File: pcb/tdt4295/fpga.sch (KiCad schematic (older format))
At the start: 44 parts, among them J101 FPGA__debug, U101 S25FL127SABMFV101, U102 XC7A100T-FTG256-tdt4295

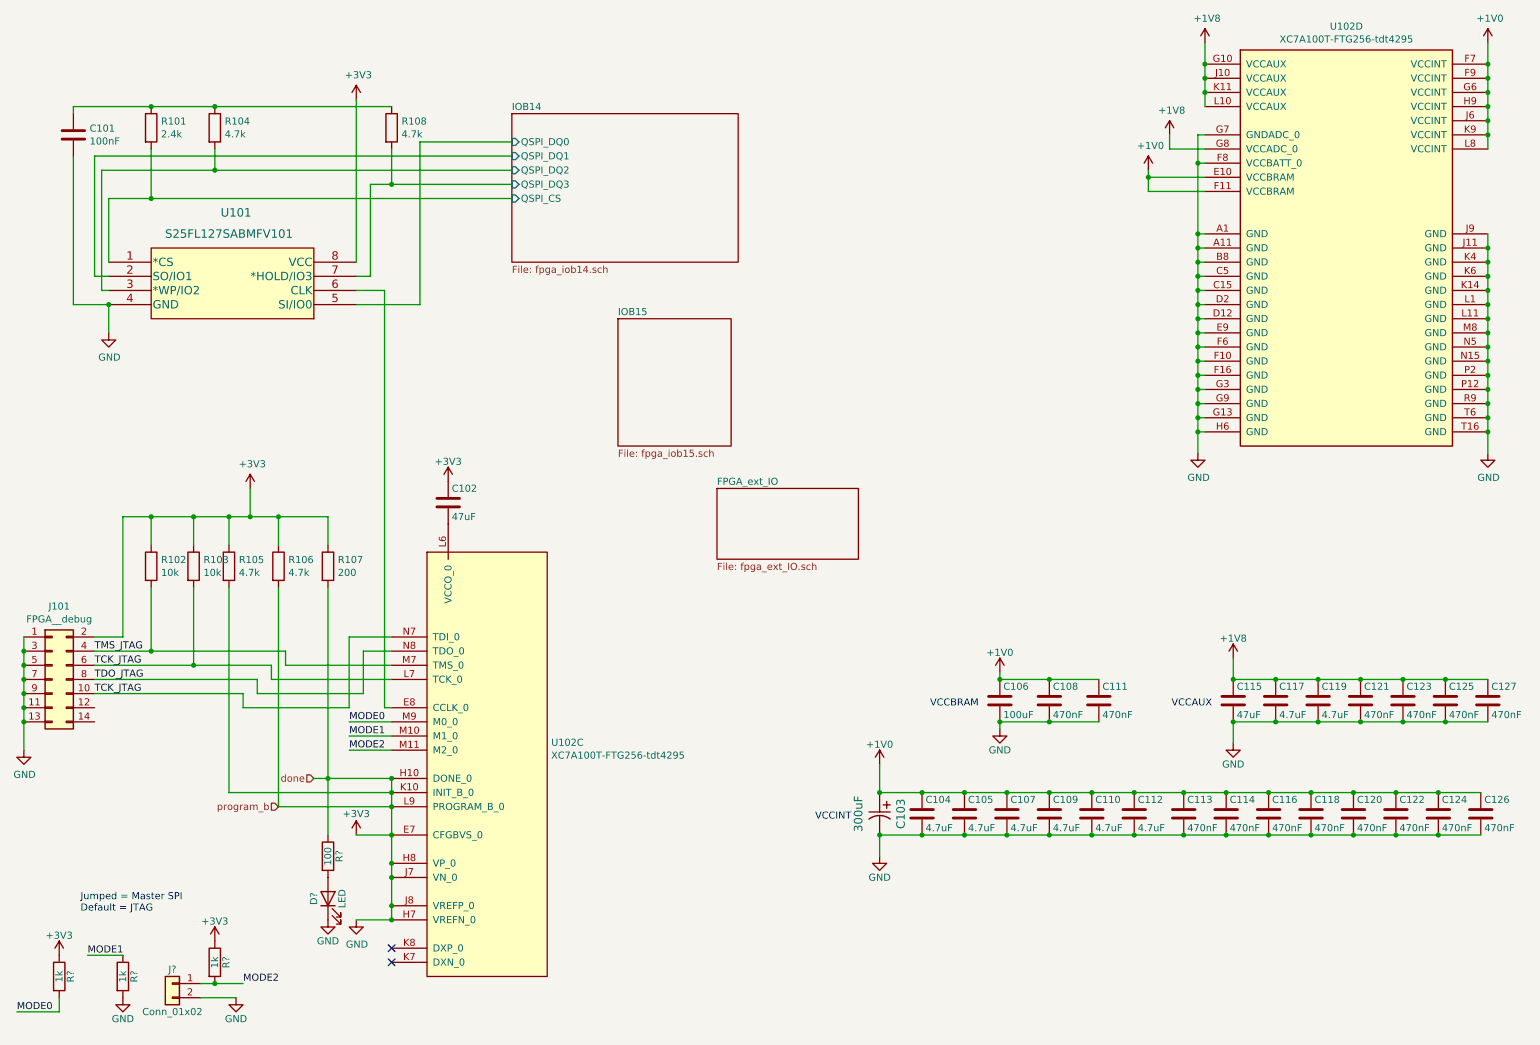
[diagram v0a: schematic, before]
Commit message: associate (most) symbols with footprints
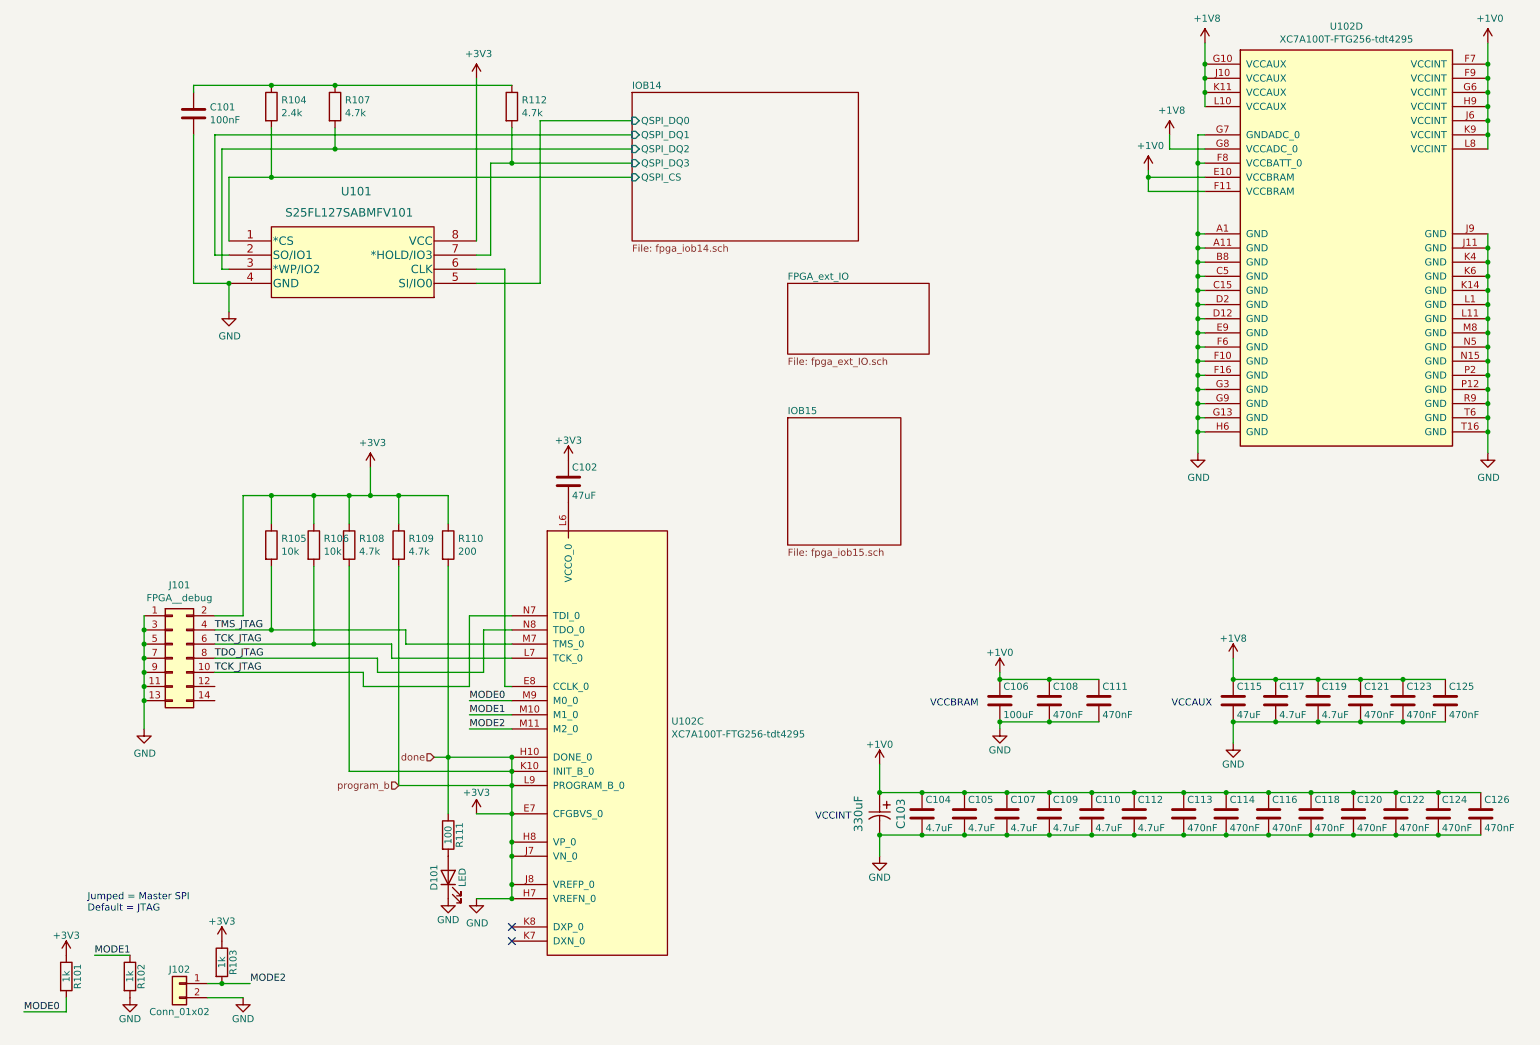
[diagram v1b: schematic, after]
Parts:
- removed C127: 470nF, symbol Device:C
- C102: footprint (none) -> Capacitor_SMD:C_1210_3225Metric_Pad1.33x2.70mm_HandSolder; Component name (none) -> GRM32ER71A476ME15L
- C103: value 300uF -> 330uF
- C108, C111, C113, C114, C116, C118, C120, C121, C122, C123, C124, C125, C126: footprint (none) -> Capacitor_SMD:C_0603_1608Metric_Pad1.08x0.95mm_HandSolder; Component name (none) -> GRM188R71C474KA88D
- D101: renamed from D?; footprint (none) -> Diode_SMD:D_0805_2012Metric_Pad1.15x1.40mm_HandSolder
- J102: renamed from J?; footprint (none) -> Connector_PinHeader_2.54mm:PinHeader_1x02_P2.54mm_Vertical
- R101, R102, R103: renamed from R?; footprint (none) -> Resistor_SMD:R_0402_1005Metric_Pad0.72x0.64mm_HandSolder; Component name (none) -> RR0510P-102-D
- R104: renamed from R101; footprint (none) -> Resistor_SMD:R_0805_2012Metric_Pad1.20x1.40mm_HandSolder; Component name (none) -> ERA-6AED242V
- R105: renamed from R102; footprint (none) -> Resistor_SMD:R_0805_2012Metric_Pad1.20x1.40mm_HandSolder; Component name (none) -> RR1220P-103-D
- R106: renamed from R103; footprint (none) -> Resistor_SMD:R_0805_2012Metric_Pad1.20x1.40mm_HandSolder; Component name (none) -> RR1220P-103-D
- R107: renamed from R104; footprint (none) -> Resistor_SMD:R_0603_1608Metric_Pad0.98x0.95mm_HandSolder; Component name (none) -> RG1608P-472-B-T5
- R108: renamed from R105; footprint (none) -> Resistor_SMD:R_0603_1608Metric_Pad0.98x0.95mm_HandSolder; Component name (none) -> RG1608P-472-B-T5
- R109: renamed from R106; footprint (none) -> Resistor_SMD:R_0603_1608Metric_Pad0.98x0.95mm_HandSolder; Component name (none) -> RG1608P-472-B-T5
- R110: renamed from R107; footprint (none) -> Resistor_SMD:R_0805_2012Metric_Pad1.20x1.40mm_HandSolder; Component name (none) -> RNCF0805TKY200R
- R111: renamed from R?; footprint (none) -> Resistor_SMD:R_0805_2012Metric_Pad1.20x1.40mm_HandSolder; Component name (none) -> TNPW0805100RBEEA
- R112: renamed from R108; footprint (none) -> Resistor_SMD:R_0603_1608Metric_Pad0.98x0.95mm_HandSolder; Component name (none) -> RG1608P-472-B-T5
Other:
- moved on the sheet: C101, C102, D101, J101, J102, R101, R102, R103, R104, R105, R106, R107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

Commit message: add final footprints, tweak VGA output
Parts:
- C101: footprint (none) -> Resistor_SMD:R_0402_1005Metric_Pad0.72x0.64mm_HandSolder; Component name (none) -> CL05B104KA5NNNC
- C103: footprint CAPMP7.6X4.3_1.9N_KEM -> T520V337M2R5ATE025-footprint:T520V337M2R5ATE025
- J101: footprint Connector_PinHeader_1.00mm:PinHeader_2x07_P1.00mm_Vertical -> Connector_PinHeader_2.54mm:PinHeader_1x02_P2.54mm_Vertical
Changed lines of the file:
@@
 F 0 "C103" H 6750 6250 60  0000 C CNN
 F 1 "330uF" H 6750 5950 60  0000 C CNN
-F 2 "CAPMP7.6X4.3_1.9N_KEM" H 6750 5740 60  0001 C CNN
+F 2 "T520V337M2R5ATE025-footprint:T520V337M2R5ATE025" H 6750 5740 60  0001 C CNN
 F 3 "" H 6600 6100 60  0000 C CNN
 F 4 "T520V337M2R5ATE025" H 6600 6100 50  0001 C CNN "Component name"
@@
 F 0 "C101" H 1865 1346 50  0000 L CNN
 F 1 "100nF" H 1865 1255 50  0000 L CNN
-F 2 "" H 1788 1150 50  0001 C CNN
-F 3 "~" H 1750 1300 50  0001 C CNN
+F 2 "Resistor_SMD:R_0402_1005Metric_Pad0.72x0.64mm_HandSolder" H 1788 1150 50  0001 C CNN
+F 3 "https://media.digikey.com/pdf/Data%20Sheets/Samsung%20PDFs/CL05B104KA5NNNC_Spec.pdf" H 1750 1300 50  0001 C CNN
+F 4 "CL05B104KA5NNNC" H 1750 1300 50  0001 C CNN "Component name"
 	1    1750 1300
 	1    0    0    -1
@@
 F 1 "S25FL127SABMFV101" H 2850 2400 60  0000 C CNN
 F 2 "S25FL127SABMFV101-footprint:S25FL127SABMFV101" H 2250 2440 60  0001 C CNN
-F 3 "" H 750 2200 60  0000 C CNN
+F 3 "https://www.cypress.com/file/177961/download" H 750 2200 60  0001 C CNN
 	1    750  2200
 	1    0    0    -1
@@
 F 0 "J101" H 1650 5667 50  0000 C CNN
 F 1 "FPGA__debug" H 1650 5576 50  0000 C CNN
-F 2 "Connector_PinHeader_1.00mm:PinHeader_2x07_P1.00mm_Vertical" H 1600 5150 50  0001 C CNN
+F 2 "Connector_PinHeader_2.54mm:PinHeader_1x02_P2.54mm_Vertical" H 1600 5150 50  0001 C CNN
 F 3 "~" H 1600 5150 50  0001 C CNN
 	1    1600 5150

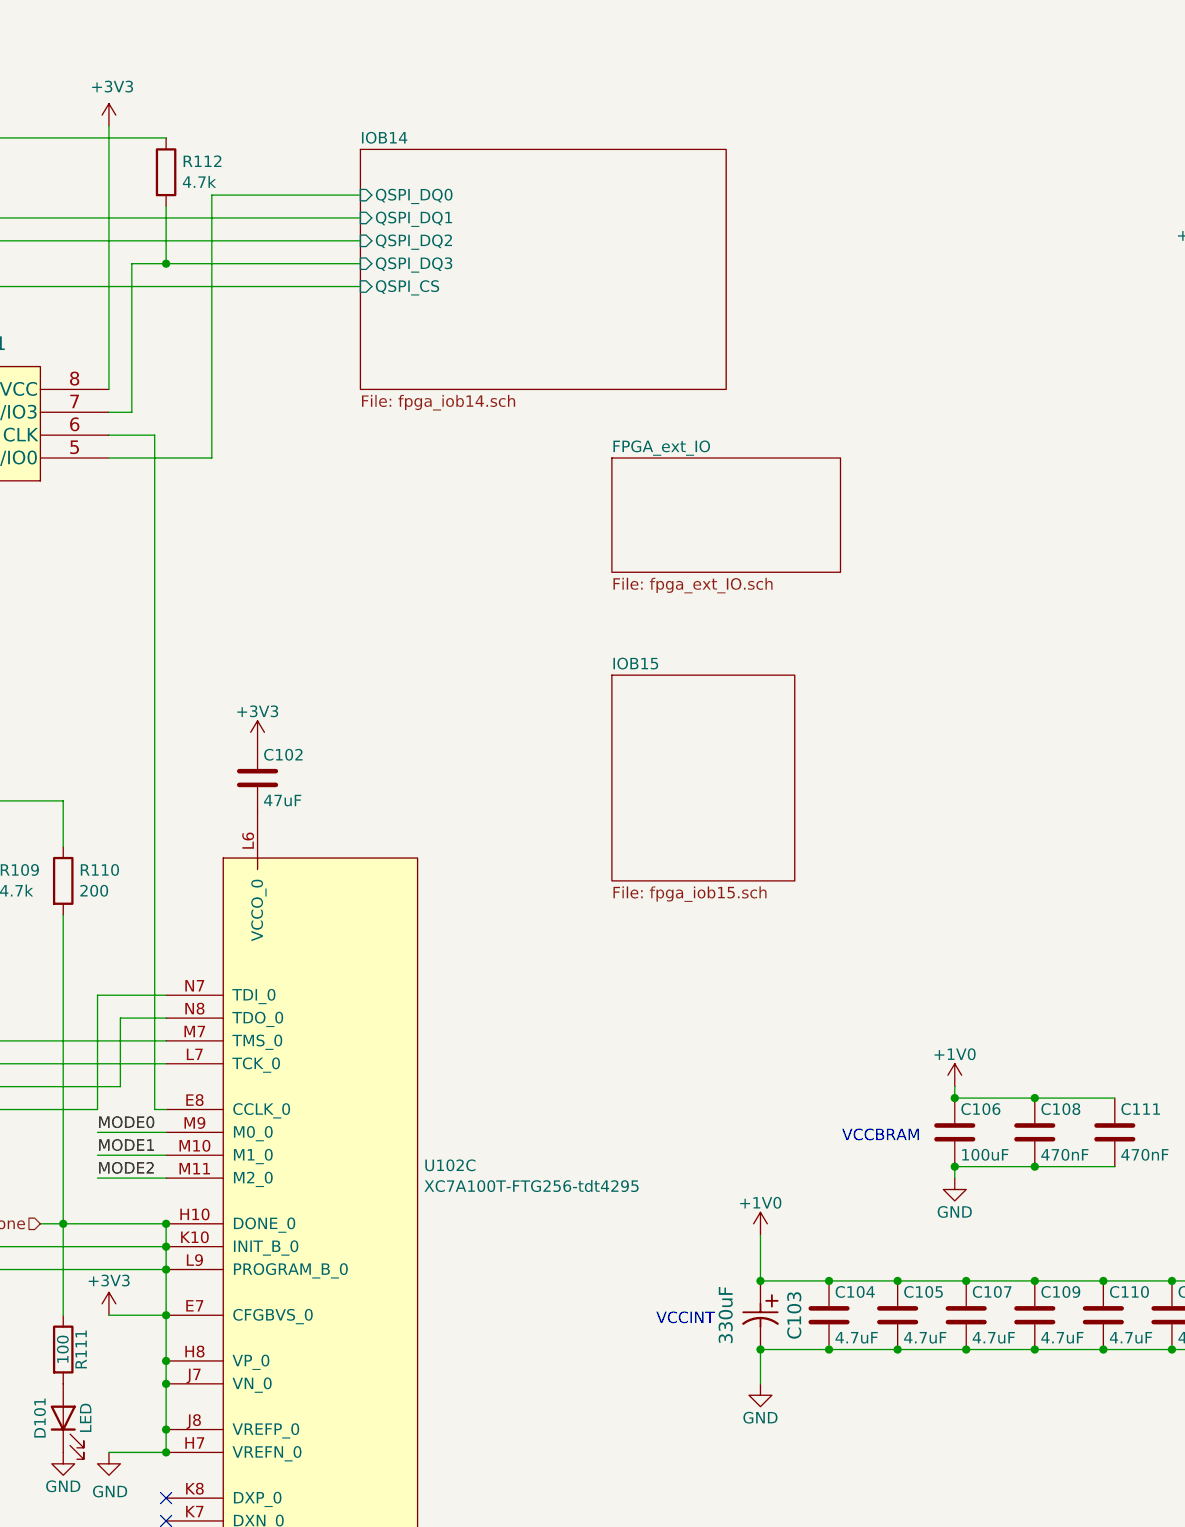
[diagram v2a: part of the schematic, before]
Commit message: delete accidental junctions
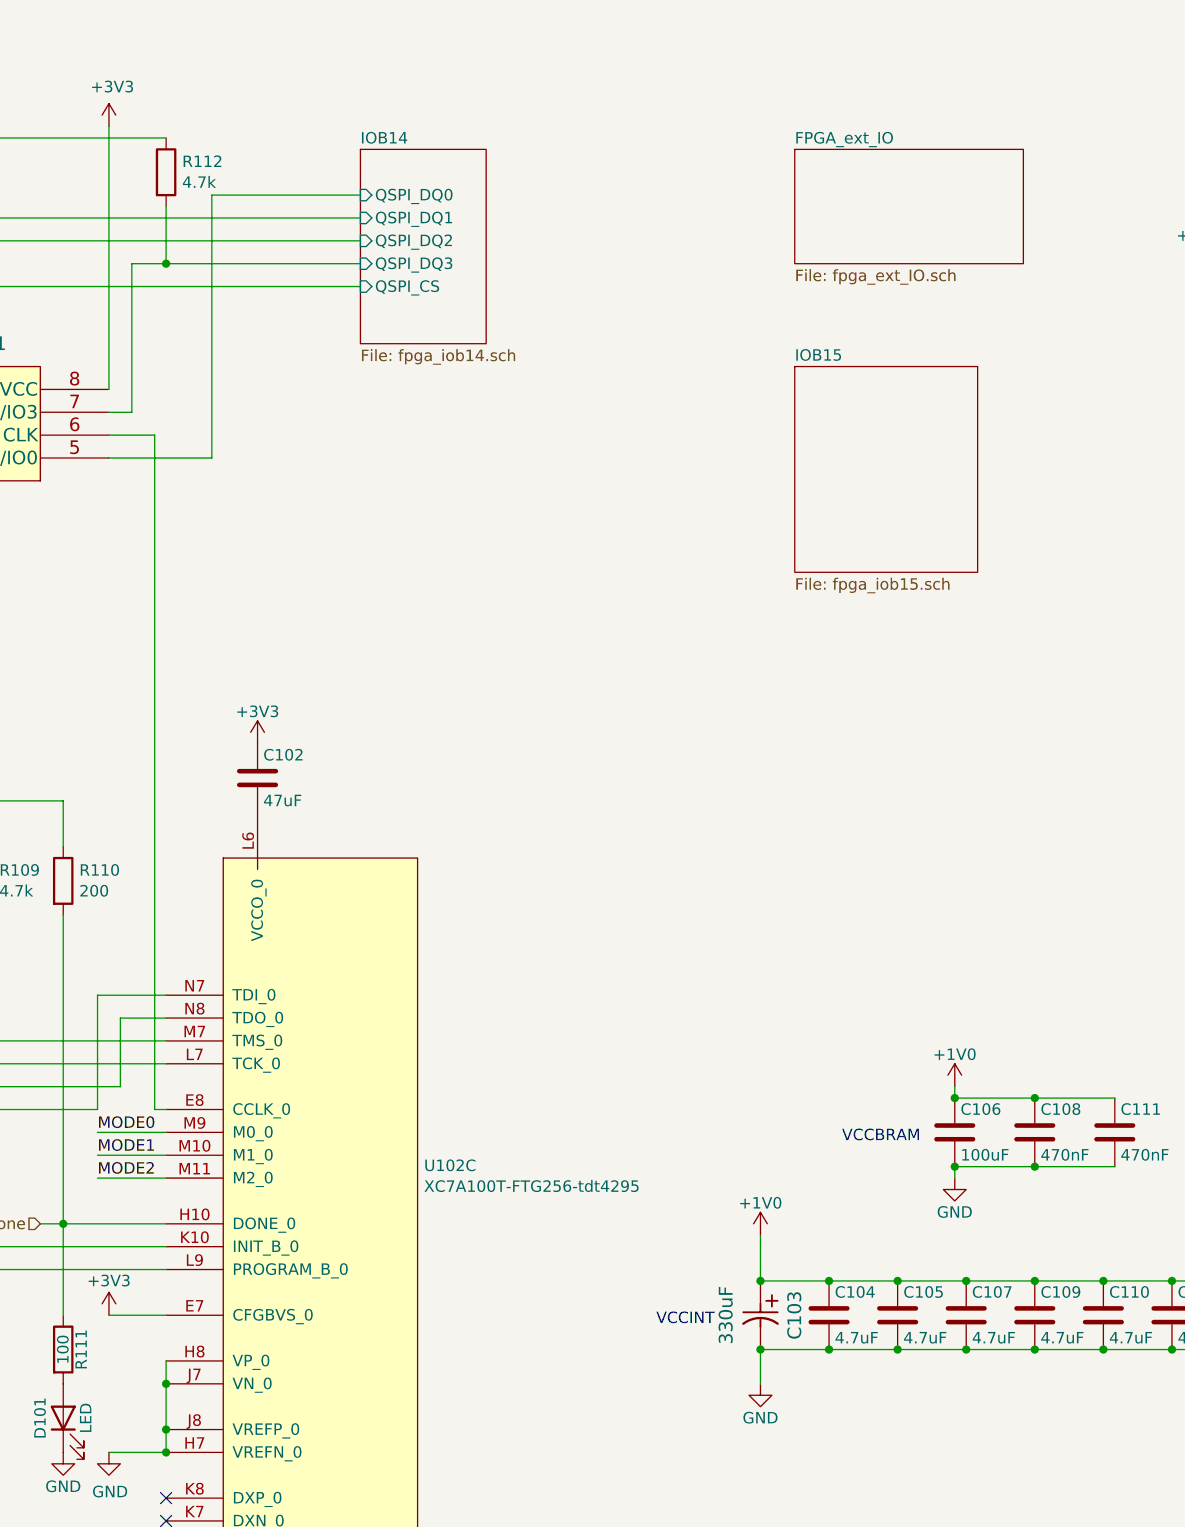
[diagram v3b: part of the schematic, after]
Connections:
- net +3V3: no longer C101.2, C103.2, C104.2, C105.2, C106.2, C107.2, C108.2, C109.2, C110.2, C111.2, C112.2, C113.2, C114.2, C115.2, C116.2, C117.2, C118.2, C119.2, C120.2, C121.2, C122.2, C123.2, C124.2, C125.2, C126.2, D101.1 (K), J101.1 (Pin_1), J101.11 (Pin_11), J101.13 (Pin_13), J101.3 (Pin_3), J101.5 (Pin_5), J101.7 (Pin_7), J101.9 (Pin_9), J102.2 (Pin_2), R102.2, R108.2, R109.2, R110.2, R111.1, U101.4 (GND), U102.A1 (GND), U102.A11 (GND), U102.B8 (GND), U102.C15 (GND), U102.C5 (GND), U102.D12 (GND), U102.D2 (GND), U102.E9 (GND), U102.F10 (GND), U102.F16 (GND), U102.F6 (GND), U102.F8 (VCCBATT_0), U102.G13 (GND), U102.G3 (GND), U102.G7 (GNDADC_0), U102.G9 (GND), U102.H10 (DONE_0), U102.H6 (GND), U102.H7 (VREFN_0), U102.H8 (VP_0), U102.J11 (GND), U102.J7 (VN_0), U102.J8 (VREFP_0), U102.J9 (GND), U102.K10 (INIT_B_0), U102.K14 (GND), U102.K4 (GND), U102.K6 (GND), U102.L1 (GND), U102.L11 (GND), U102.L9 (PROGRAM_B_0), U102.M8 (GND), U102.N15 (GND), U102.N5 (GND), U102.P12 (GND), U102.P2 (GND), U102.R9 (GND), U102.T16 (GND), U102.T6 (GND)
- new net: R108.2, U102.K10 (INIT_B_0)
- new net GND: C101.2, C103.2, C104.2, C105.2, C106.2, C107.2, C108.2, C109.2, C110.2, C111.2, C112.2, C113.2, C114.2, C115.2, C116.2, C117.2, C118.2, C119.2, C120.2, C121.2, C122.2, C123.2, C124.2, C125.2, C126.2, D101.1 (K), J101.1 (Pin_1), J101.11 (Pin_11), J101.13 (Pin_13), J101.3 (Pin_3), J101.5 (Pin_5), J101.7 (Pin_7), J101.9 (Pin_9), J102.2 (Pin_2), R102.2, U101.4 (GND), U102.A1 (GND), U102.A11 (GND), U102.B8 (GND), U102.C15 (GND), U102.C5 (GND), U102.D12 (GND), U102.D2 (GND), U102.E9 (GND), U102.F10 (GND), U102.F16 (GND), U102.F6 (GND), U102.F8 (VCCBATT_0), U102.G13 (GND), U102.G3 (GND), U102.G7 (GNDADC_0), U102.G9 (GND), U102.H6 (GND), U102.H7 (VREFN_0), U102.H8 (VP_0), U102.J11 (GND), U102.J7 (VN_0), U102.J8 (VREFP_0), U102.J9 (GND), U102.K14 (GND), U102.K4 (GND), U102.K6 (GND), U102.L1 (GND), U102.L11 (GND), U102.M8 (GND), U102.N15 (GND), U102.N5 (GND), U102.P12 (GND), U102.P2 (GND), U102.R9 (GND), U102.T16 (GND), U102.T6 (GND)
- new net done: R110.2, R111.1, U102.H10 (DONE_0)
- new net program_b: R109.2, U102.L9 (PROGRAM_B_0)
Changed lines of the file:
@@
 $EndComp
 $Sheet
-S 5950 3450 800  900
+S 6750 2100 800  900
 U 614933B1
 F0 "IOB15" 50
@@
 $EndSheet
 $Sheet
-S 5950 2500 1000 500
+S 6750 1150 1000 500
 U 61537853
 F0 "FPGA_ext_IO" 50
@@
 $EndComp
 $Sheet
-S 4850 1150 1600 1050
+S 4850 1150 550  850
 U 61459CB7
 F0 "IOB14" 50
@@
 Wire Wire Line
 	4000 6450 4000 6550
-Connection ~ 4000 6450
-Wire Wire Line
-	4000 6250 4000 6450
-Connection ~ 4000 6250
-Wire Wire Line
-	4000 6050 4000 6250
-Connection ~ 4000 6050
-Wire Wire Line
-	4000 5950 4000 6050
-Connection ~ 4000 5950
-Wire Wire Line
-	4000 5850 4000 5950
-Connection ~ 4000 5850
 Wire Wire Line
 	2000 1750 2300 1750
